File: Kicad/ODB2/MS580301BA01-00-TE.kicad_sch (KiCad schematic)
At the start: 2 parts, among them U7 MS580301BA01-00

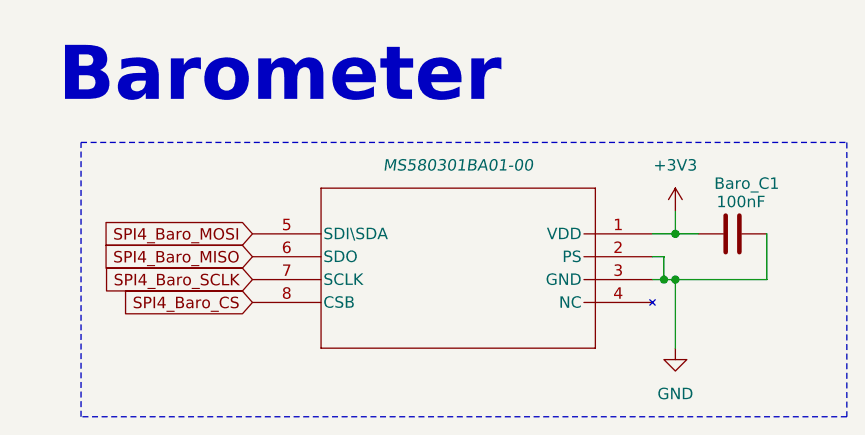
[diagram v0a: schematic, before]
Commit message: merge all sensors to main page + fix NC
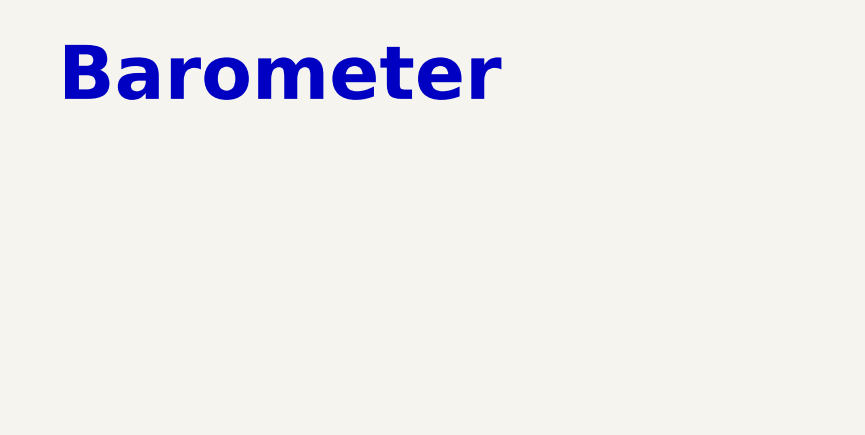
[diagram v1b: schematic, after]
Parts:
- removed Baro_C1: 100nF, symbol Device:C
- removed U7: MS580301BA01-00, MS5803-01BA01_TEC, symbol ODB_Lib:MS580301BA01-00
